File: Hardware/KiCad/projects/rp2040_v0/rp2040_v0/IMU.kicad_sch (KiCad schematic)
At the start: 16 parts, among them J13 Conn_02x12_Odd_Even, U5 BMI088

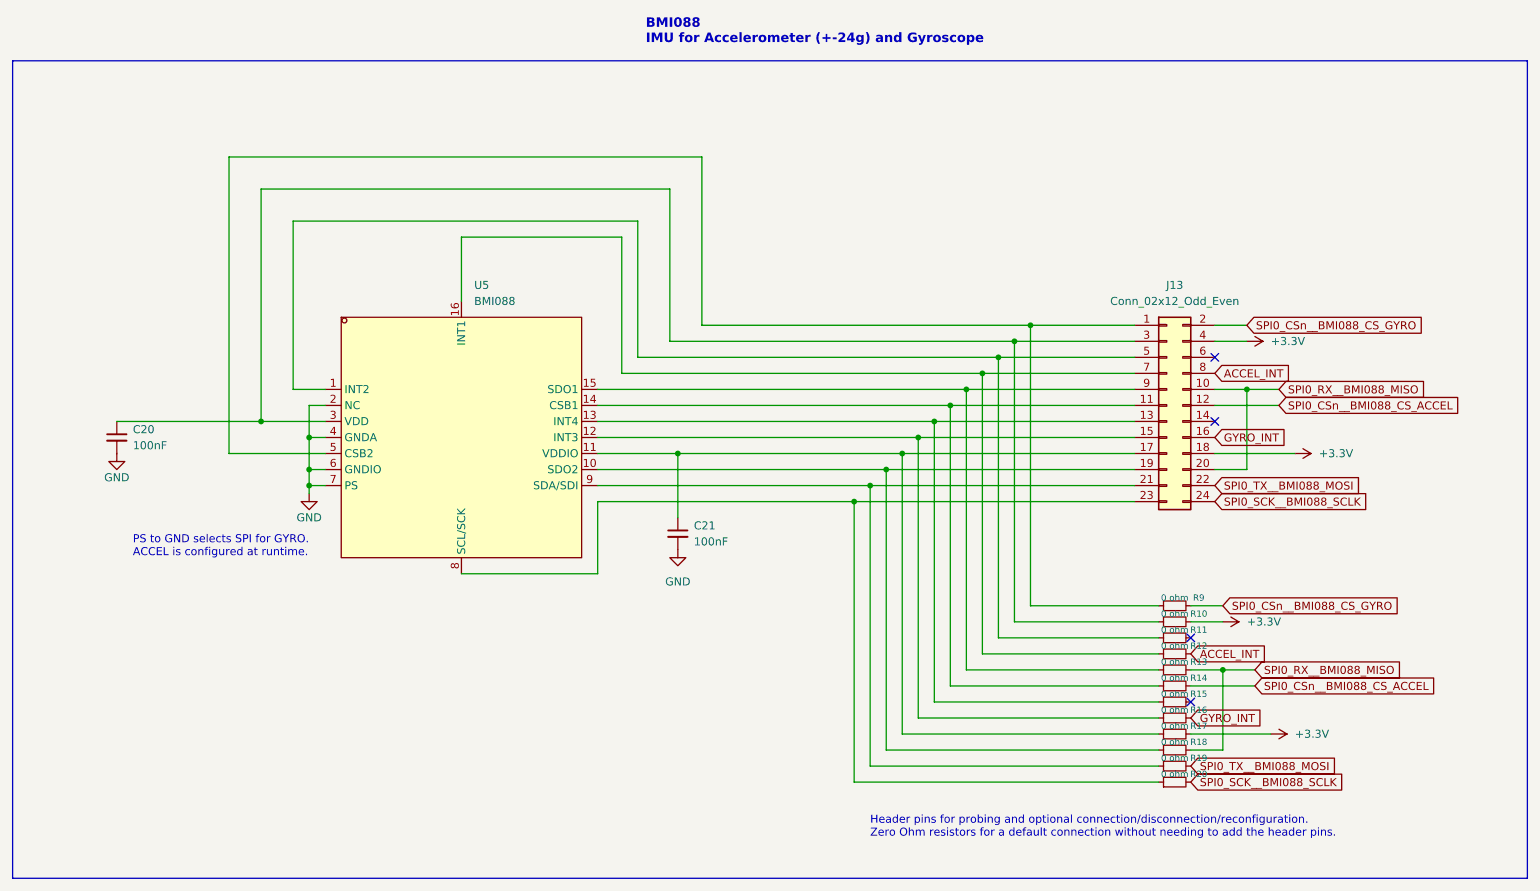
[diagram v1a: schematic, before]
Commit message: Make the IMU header smaller
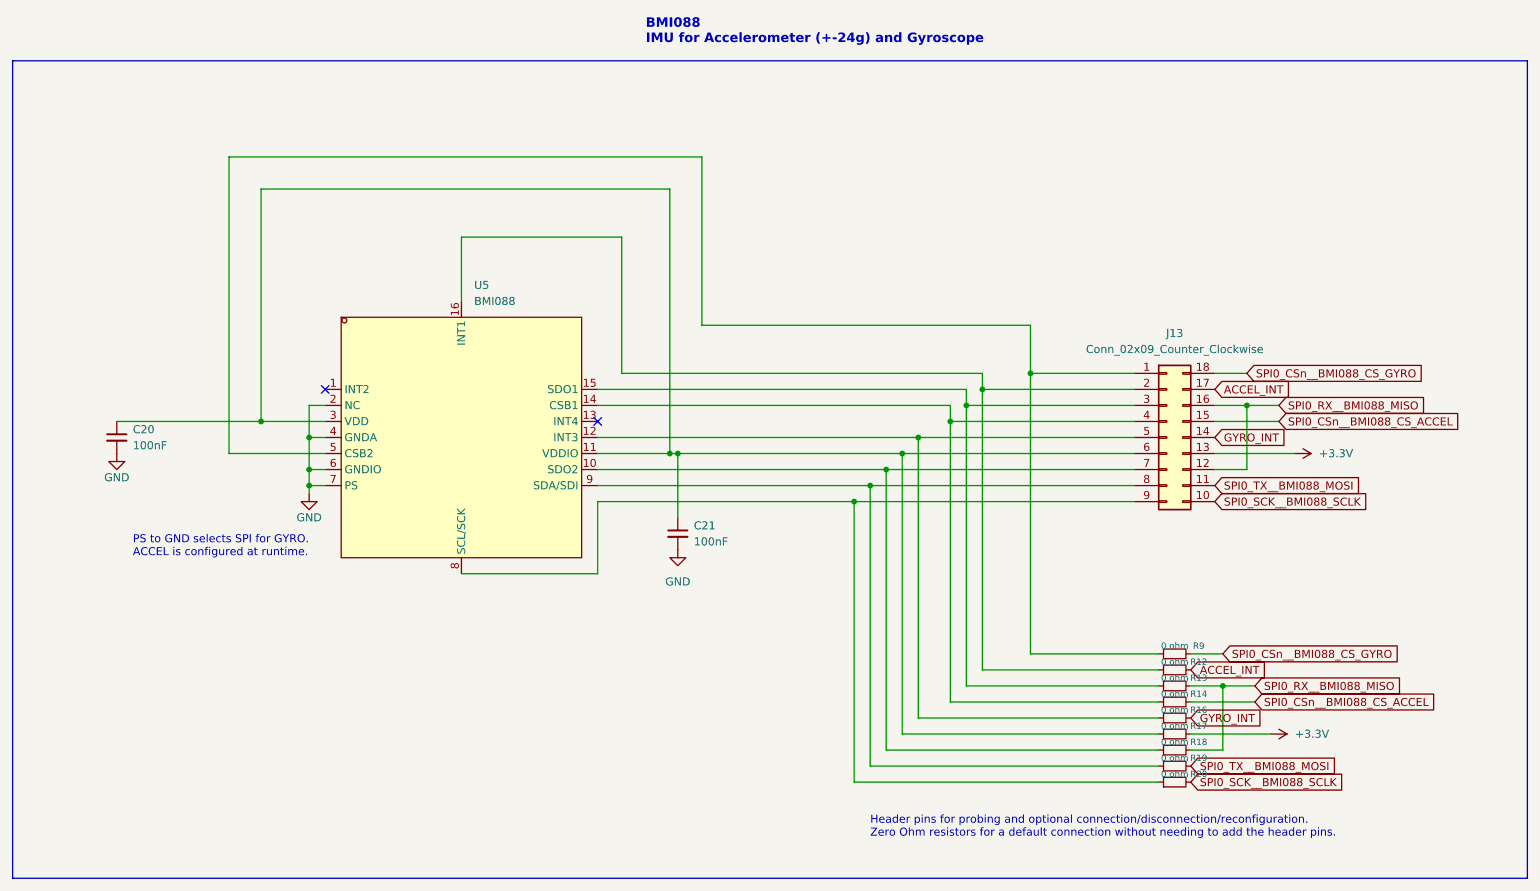
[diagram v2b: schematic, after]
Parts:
- removed J13: Conn_02x12_Odd_Even, Connector_PinHeader_2.54mm:PinHeader_2x12_P2.54mm_Vertical, symbol Connector_Generic:Conn_02x12_Odd_Even
- removed R10, R11, R15: 0 ohm, Resistor_SMD:R_0402_1005Metric, symbol Device:R_Small
- added J13: Conn_02x09_Counter_Clockwise, Connector_PinHeader_2.54mm:PinHeader_2x09_P2.54mm_Vertical, symbol Connector_Generic:Conn_02x09_Counter_Clockwise
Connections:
- net +3.3V: now also J13.13 (Pin_13)
- net ACCEL_INT: now also J13.17 (Pin_17)
- net GYRO_INT: now also J13.14 (Pin_14)
- net SPI0_CSn__BMI088_CS_ACCEL: now also J13.15 (Pin_15)
- net SPI0_CSn__BMI088_CS_GYRO: now also J13.18 (Pin_18)
- net SPI0_RX__BMI088_MISO: now also J13.12 (Pin_12), J13.16 (Pin_16)
- net SPI0_SCK__BMI088_SCLK: now also J13.10 (Pin_10)
- net SPI0_TX__BMI088_MOSI: now also J13.11 (Pin_11)
- net at R18.1, U5.10 (SDO2): now also J13.7 (Pin_7)
- net at R9.1, U5.5 (CSB2): now also J13.1 (Pin_1)
- net at R14.1, U5.14 (CSB1): now also J13.4 (Pin_4)
- net at R16.1, U5.12 (INT3): now also J13.5 (Pin_5)
- net at C21.1, R17.1, U5.11 (VDDIO): now also C20.1, U5.3 (VDD), J13.6 (Pin_6)
- net at R19.1, U5.9 (SDA/SDI): now also J13.8 (Pin_8)
- net at R20.1, U5.8 (SCL/SCK): now also J13.9 (Pin_9)
- net at R12.1, U5.16 (INT1): now also J13.2 (Pin_2)
- net at R13.1, U5.15 (SDO1): now also J13.3 (Pin_3)
- no-connect marks 4 -> 2
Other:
- moved on the sheet: R12, R13, R14, R9

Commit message: Delete and readd old components to appease the DRC
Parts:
- removed U5: BMI088, easyeda2kicad:LGA-16_L4.5-W3.0-P0.50-BL, symbol easyeda2kicad:BMI088
- added U5: BMI088, easyeda2kicad:LGA-16_L4.5-W3.0-P0.50-BL, symbol easyeda2kicad_flight_computer:BMI088
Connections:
- net GND: now also U5.2 (NC), U5.4 (GNDA), U5.6 (GNDIO), U5.7 (PS)
- net at J13.7 (Pin_7), R18.1: now also U5.10 (SDO2)
- net at J13.2 (Pin_2), R12.1: now also U5.16 (INT1)
- net at J13.3 (Pin_3), R13.1: now also U5.15 (SDO1)
- net at C20.1, C21.1, J13.6 (Pin_6)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: now also U5.11 (VDDIO), U5.3 (VDD)
- net at J13.9 (Pin_9), R20.1: now also U5.8 (SCL/SCK)
- net at J13.5 (Pin_5), R16.1: now also U5.12 (INT3)
- net at J13.4 (Pin_4), R14.1: now also U5.14 (CSB1)
- net at J13.1 (Pin_1), R9.1: now also U5.5 (CSB2)
- net at J13.8 (Pin_8), R19.1: now also U5.9 (SDA/SDI)
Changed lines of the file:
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@@
     (pin "2")
+  )
+  (symbol (lib_id "easyeda2kicad_flight_computer:BMI088") (at 111.76 91.44 0) (unit 1)
+    (in_bom yes) (on_board yes) (fields_autoplaced)
+    (property "Reference" "U5" (id 0) (at 113.7794 67.31 0)
+      (effects (font (size 1.27 1.27)) (justify left))
+    )
+    (property "Value" "BMI088" (id 1) (at 113.7794 69.85 0)
+      (effects (font (size 1.27 1.27)) (justify left))
+    )
+    (property "Footprint" "easyeda2kicad:LGA-16_L4.5-W3.0-P0.50-BL" (id 2) (at 111.76 120.65 0)
+      (effects (font (size 1.27 1.27)) hide)
+    )
+    (property "Datasheet" "https://lcsc.com/product-detail/Others_Bosch-Sensortec_BMI088_Bosch-Sensortec-BMI088_C194919.html" (id 3) (at 111.76 123.19 0)
+      (effects (font (size 1.27 1.27)) hide)
+    )
+    (property "Manufacturer" "Bosch(博世)" (id 4) (at 111.76 125.73 0)
+      (effects (font (size 1.27 1.27)) hide)
+    )
+    (property "LCSC Part" "C194919" (id 5) (at 111.76 128.27 0)
+      (effects (font (size 1.27 1.27)) hide)
+    )
+    (property "JLC Part" "Extended Part" (id 6) (at 111.76 130.81 0)
+      (effects (font (size 1.27 1.27)) hide)
+    )
+    (pin "1")
+    (pin "10")
+    (pin "11")
+    (pin "12")
+    (pin "13")
+    (pin "14")
+    (pin "15")
+    (pin "16")
+    (pin "2")
+    (pin "3")
+    (pin "4")
+    (pin "5")
+    (pin "6")
+    (pin "7")
+    (pin "8")
+    (pin "9")
   )
   (symbol (lib_id "Device:R_Small") (at 224.79 130.81 90) (unit 1)
@@
     (pin "2")
   )
-  (symbol (lib_id "easyeda2kicad:BMI088") (at 111.76 91.44 0) (unit 1)
-    (in_bom yes) (on_board yes) (fields_autoplaced)
-    (property "Reference" "U5" (id 0) (at 113.7794 67.31 0)
-      (effects (font (size 1.27 1.27)) (justify left))
-    )
-    (property "Value" "BMI088" (id 1) (at 113.7794 69.85 0)
-      (effects (font (size 1.27 1.27)) (justify left))
-    )
-    (property "Footprint" "easyeda2kicad:LGA-16_L4.5-W3.0-P0.50-BL" (id 2) (at 111.76 120.65 0)
-      (effects (font (size 1.27 1.27)) hide)
-    )
-    (property "Datasheet" "https://lcsc.com/product-detail/Others_Bosch-Sensortec_BMI088_Bosch-Sensortec-BMI088_C194919.html" (id 3) (at 111.76 123.19 0)
-      (effects (font (size 1.27 1.27)) hide)
-    )
-    (property "Manufacturer" "Bosch(博世)" (id 4) (at 111.76 125.73 0)
-      (effects (font (size 1.27 1.27)) hide)
-    )
-    (property "LCSC Part" "C194919" (id 5) (at 111.76 128.27 0)
-      (effects (font (size 1.27 1.27)) hide)
-    )
-    (property "JLC Part" "Extended Part" (id 6) (at 111.76 130.81 0)
-      (effects (font (size 1.27 1.27)) hide)
-    )
-    (pin "1")
-    (pin "10")
-    (pin "11")
-    (pin "12")
-    (pin "13")
-    (pin "14")
-    (pin "15")
-    (pin "16")
-    (pin "2")
-    (pin "3")
-    (pin "4")
-    (pin "5")
-    (pin "6")
-    (pin "7")
-    (pin "8")
-    (pin "9")
-  )
   (symbol (lib_id "Device:R_Small") (at 224.79 133.35 90) (unit 1)
